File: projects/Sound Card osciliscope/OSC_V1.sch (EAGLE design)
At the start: 11 parts, among them X1 22-23-2021, X2 22-23-2021

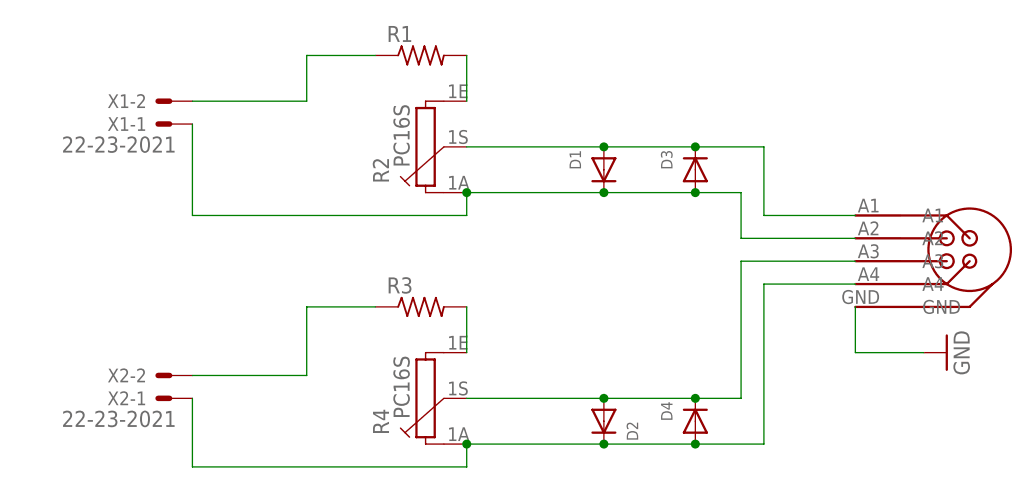
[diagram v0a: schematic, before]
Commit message: Update Library and Sccope
Added 3pin Jack to Library and finished up with the osciliscope
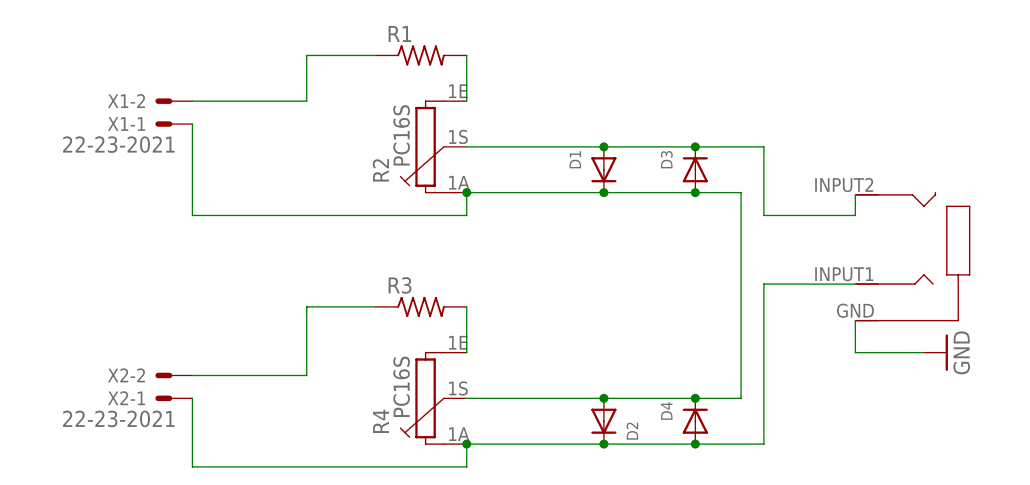
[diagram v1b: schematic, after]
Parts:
- U$1: value AUDIO5PIN -> AUDIO3PIN; device Test:AUDIO5PIN -> Test:AUDIO3PIN; OC_NEWARK unknown -> (none)
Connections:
- removed net N$7: D2.A, D4.C, R4.1S, U$1.A3
- net GND: now also D2.A, D4.C, R4.1S; no longer U$1.A2
- net N$3: now also U$1.INPUT2; no longer U$1.A1
- net N$8: now also U$1.INPUT1; no longer U$1.A4
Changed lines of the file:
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@@
-<attribute name="OC_NEWARK" value="unknown"/>
-</part>
-<part name="U$1" library="Test" deviceset="AUDIO5PIN" device="">
-<attribute name="MF" value=""/>
-<attribute name="MPN" value=""/>
 <attribute name="OC_NEWARK" value="unknown"/>
 </part>
@@
 <attribute name="OC_NEWARK" value="unknown"/>
 </part>
+<part name="U$1" library="Test" deviceset="AUDIO3PIN" device=""/>
 </parts>
 <sheets>
@@
 <attribute name="MPN" x="96.52" y="45.72" size="1.778" layer="96" display="off"/>
 </instance>
-<instance part="U$1" gate="G$1" x="127" y="63.5" smashed="yes">
-<attribute name="OC_NEWARK" x="127" y="63.5" size="1.778" layer="96" display="off"/>
-<attribute name="MF" x="127" y="63.5" size="1.778" layer="96" display="off"/>
-<attribute name="MPN" x="127" y="63.5" size="1.778" layer="96" display="off"/>
-</instance>
 <instance part="GND1" gate="1" x="124.46" y="53.34" smashed="yes" rot="R90">
 <attribute name="VALUE" x="127" y="50.8" size="1.778" layer="96" rot="R90"/>
@@
 <attribute name="MPN" x="86.36" y="45.72" size="1.778" layer="96" display="off"/>
 </instance>
+<instance part="U$1" gate="G$1" x="127" y="71.12" smashed="yes" rot="R180"/>
 </instances>
 <busses>
@@
 <net name="GND" class="0">
 <segment>
-<pinref part="U$1" gate="G$1" pin="GND"/>
-<wire x1="114.3" y1="58.42" x2="114.3" y2="53.34" width="0.1524" layer="91"/>
+<wire x1="114.3" y1="56.896" x2="114.3" y2="53.34" width="0.1524" layer="91"/>
 <wire x1="114.3" y1="53.34" x2="121.92" y2="53.34" width="0.1524" layer="91"/>
 <pinref part="GND1" gate="1" pin="GND"/>
+<pinref part="U$1" gate="G$1" pin="GND"/>
 </segment>
 <segment>
@@
 <wire x1="86.36" y1="71.12" x2="96.52" y2="71.12" width="0.1524" layer="91"/>
 <wire x1="96.52" y1="71.12" x2="101.6" y2="71.12" width="0.1524" layer="91"/>
-<wire x1="101.6" y1="71.12" x2="101.6" y2="66.04" width="0.1524" layer="91"/>
 <junction x="71.12" y="71.12"/>
-<pinref part="U$1" gate="G$1" pin="A2"/>
-<wire x1="101.6" y1="66.04" x2="114.3" y2="66.04" width="0.1524" layer="91"/>
 <pinref part="D1" gate="G$1" pin="C"/>
 <junction x="86.36" y="71.12"/>
 <pinref part="D3" gate="G$1" pin="A"/>
 <junction x="96.52" y="71.12"/>
-</segment>
-</net>
-<net name="N$1" class="0">
-<segment>
-<pinref part="X1" gate="-2" pin="S"/>
-<wire x1="40.64" y1="81.28" x2="53.34" y2="81.28" width="0.1524" layer="91"/>
-<wire x1="53.34" y1="81.28" x2="53.34" y2="86.36" width="0.1524" layer="91"/>
-<pinref part="R1" gate="G$1" pin="1"/>
-<wire x1="53.34" y1="86.36" x2="60.96" y2="86.36" width="0.1524" layer="91"/>
-</segment>
-</net>
-<net name="N$2" class="0">
-<segment>
-<pinref part="R1" gate="G$1" pin="2"/>
-<pinref part="R2" gate="G$1" pin="1E"/>
-<wire x1="71.12" y1="86.36" x2="71.12" y2="81.28" width="0.1524" layer="91"/>
-</segment>
-</net>
-<net name="N$3" class="0">
-<segment>
-<pinref part="R2" gate="G$1" pin="1S"/>
-<wire x1="71.12" y1="76.2" x2="86.36" y2="76.2" width="0.1524" layer="91"/>
-<wire x1="86.36" y1="76.2" x2="96.52" y2="76.2" width="0.1524" layer="91"/>
-<wire x1="96.52" y1="76.2" x2="104.14" y2="76.2" width="0.1524" layer="91"/>
-<wire x1="104.14" y1="76.2" x2="104.14" y2="68.58" width="0.1524" layer="91"/>
-<pinref part="U$1" gate="G$1" pin="A1"/>
-<wire x1="104.14" y1="68.58" x2="114.3" y2="68.58" width="0.1524" layer="91"/>
-<pinref part="D1" gate="G$1" pin="A"/>
-<junction x="86.36" y="76.2"/>
-<pinref part="D3" gate="G$1" pin="C"/>
-<junction x="96.52" y="76.2"/>
-</segment>
-</net>
-<net name="N$5" class="0">
-<segment>
-<pinref part="X2" gate="-2" pin="S"/>
-<wire x1="40.64" y1="50.8" x2="53.34" y2="50.8" width="0.1524" layer="91"/>
-<wire x1="53.34" y1="50.8" x2="53.34" y2="58.42" width="0.1524" layer="91"/>
-<pinref part="R3" gate="G$1" pin="1"/>
-<wire x1="53.34" y1="58.42" x2="60.96" y2="58.42" width="0.1524" layer="91"/>
-</segment>
-</net>
-<net name="N$6" class="0">
-<segment>
-<pinref part="R3" gate="G$1" pin="2"/>
-<pinref part="R4" gate="G$1" pin="1E"/>
-<wire x1="71.12" y1="58.42" x2="71.12" y2="53.34" width="0.1524" layer="91"/>
-</segment>
-</net>
-<net name="N$7" class="0">
-<segment>
 <pinref part="R4" gate="G$1" pin="1S"/>
 <pinref part="D2" gate="G$1" pin="A"/>
@@
 <junction x="86.36" y="48.26"/>
 <wire x1="96.52" y1="48.26" x2="101.6" y2="48.26" width="0.1524" layer="91"/>
-<wire x1="101.6" y1="48.26" x2="101.6" y2="63.5" width="0.1524" layer="91"/>
+<wire x1="101.6" y1="48.26" x2="101.6" y2="71.12" width="0.1524" layer="91"/>
 <junction x="96.52" y="48.26"/>
-<pinref part="U$1" gate="G$1" pin="A3"/>
-<wire x1="101.6" y1="63.5" x2="114.3" y2="63.5" width="0.1524" layer="91"/>
+</segment>
+</net>
+<net name="N$1" class="0">
+<segment>
+<pinref part="X1" gate="-2" pin="S"/>
+<wire x1="40.64" y1="81.28" x2="53.34" y2="81.28" width="0.1524" layer="91"/>
+<wire x1="53.34" y1="81.28" x2="53.34" y2="86.36" width="0.1524" layer="91"/>
+<pinref part="R1" gate="G$1" pin="1"/>
+<wire x1="53.34" y1="86.36" x2="60.96" y2="86.36" width="0.1524" layer="91"/>
+</segment>
+</net>
+<net name="N$2" class="0">
+<segment>
+<pinref part="R1" gate="G$1" pin="2"/>
+<pinref part="R2" gate="G$1" pin="1E"/>
+<wire x1="71.12" y1="86.36" x2="71.12" y2="81.28" width="0.1524" layer="91"/>
+</segment>
+</net>
+<net name="N$3" class="0">
+<segment>
+<pinref part="R2" gate="G$1" pin="1S"/>
+<wire x1="71.12" y1="76.2" x2="86.36" y2="76.2" width="0.1524" layer="91"/>
+<wire x1="86.36" y1="76.2" x2="96.52" y2="76.2" width="0.1524" layer="91"/>
+<wire x1="96.52" y1="76.2" x2="104.14" y2="76.2" width="0.1524" layer="91"/>
+<wire x1="104.14" y1="76.2" x2="104.14" y2="68.58" width="0.1524" layer="91"/>
+<wire x1="104.14" y1="68.58" x2="114.3" y2="68.58" width="0.1524" layer="91"/>
+<pinref part="D1" gate="G$1" pin="A"/>
+<junction x="86.36" y="76.2"/>
+<pinref part="D3" gate="G$1" pin="C"/>
+<junction x="96.52" y="76.2"/>
+<pinref part="U$1" gate="G$1" pin="INPUT2"/>
+<wire x1="114.3" y1="68.58" x2="114.3" y2="70.866" width="0.1524" layer="91"/>
+</segment>
+</net>
+<net name="N$5" class="0">
+<segment>
+<pinref part="X2" gate="-2" pin="S"/>
+<wire x1="40.64" y1="50.8" x2="53.34" y2="50.8" width="0.1524" layer="91"/>
+<wire x1="53.34" y1="50.8" x2="53.34" y2="58.42" width="0.1524" layer="91"/>
+<pinref part="R3" gate="G$1" pin="1"/>
+<wire x1="53.34" y1="58.42" x2="60.96" y2="58.42" width="0.1524" layer="91"/>
+</segment>
+</net>
+<net name="N$6" class="0">
+<segment>
+<pinref part="R3" gate="G$1" pin="2"/>
+<pinref part="R4" gate="G$1" pin="1E"/>
+<wire x1="71.12" y1="58.42" x2="71.12" y2="53.34" width="0.1524" layer="91"/>
 </segment>
 </net>
@@
 <wire x1="96.52" y1="43.18" x2="104.14" y2="43.18" width="0.1524" layer="91"/>
 <wire x1="104.14" y1="43.18" x2="104.14" y2="60.96" width="0.1524" layer="91"/>
-<pinref part="U$1" gate="G$1" pin="A4"/>
 <wire x1="104.14" y1="60.96" x2="114.3" y2="60.96" width="0.1524" layer="91"/>
 <pinref part="D4" gate="G$1" pin="A"/>
@@
 <wire x1="71.12" y1="40.64" x2="71.12" y2="43.18" width="0.1524" layer="91"/>
 <junction x="71.12" y="43.18"/>
+<pinref part="U$1" gate="G$1" pin="INPUT1"/>
 </segment>
 </net>
@@
 packages will not be understood (or retained) with this version.
 </note>
-<note version="8.5" severity="warning">
-Since Version 8.5, EAGLE supports locking for holes, vias, wires and polygons.
-The locking property on all objects of these types will not be understood in this version.
-</note>
 </compatibility>

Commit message: Updated board
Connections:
- net GND: now also D2.C, D4.A, R4.1A, X2-1.S; no longer D2.A, D4.C, R4.1S
- net N$8: now also D2.A, D4.C, R4.1S; no longer D2.C, D4.A, R4.1A, X2-1.S
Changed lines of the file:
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@@
 <setting verticaltext="up"/>
 </settings>
-<grid distance="0.1" unitdist="inch" unit="inch" style="lines" multiple="1" display="no" altdistance="0.01" altunitdist="inch" altunit="inch"/>
+<grid distance="0.1" unitdist="inch" unit="inch" style="lines" multiple="1" display="yes" altdistance="0.01" altunitdist="inch" altunit="inch"/>
 <layers>
 <layer number="1" name="Top" color="4" fill="1" visible="no" active="no"/>
@@
 <net name="GND" class="0">
 <segment>
-<wire x1="114.3" y1="56.896" x2="114.3" y2="53.34" width="0.1524" layer="91"/>
+<wire x1="114.3" y1="56.896" x2="114.3" y2="55.88" width="0.1524" layer="91"/>
+<wire x1="114.3" y1="55.88" x2="114.3" y2="53.34" width="0.1524" layer="91"/>
 <wire x1="114.3" y1="53.34" x2="121.92" y2="53.34" width="0.1524" layer="91"/>
 <pinref part="GND1" gate="1" pin="GND"/>
 <pinref part="U$1" gate="G$1" pin="GND"/>
-</segment>
-<segment>
 <pinref part="X1" gate="-1" pin="S"/>
-<wire x1="40.64" y1="78.74" x2="40.64" y2="68.58" width="0.1524" layer="91"/>
-<wire x1="40.64" y1="68.58" x2="71.12" y2="68.58" width="0.1524" layer="91"/>
+<wire x1="40.64" y1="78.74" x2="48.26" y2="78.74" width="0.1524" layer="91"/>
+<wire x1="48.26" y1="78.74" x2="48.26" y2="68.58" width="0.1524" layer="91"/>
 <pinref part="R2" gate="G$1" pin="1A"/>
+<wire x1="48.26" y1="68.58" x2="71.12" y2="68.58" width="0.1524" layer="91"/>
 <wire x1="71.12" y1="68.58" x2="71.12" y2="71.12" width="0.1524" layer="91"/>
 <wire x1="71.12" y1="71.12" x2="86.36" y2="71.12" width="0.1524" layer="91"/>
 <wire x1="86.36" y1="71.12" x2="96.52" y2="71.12" width="0.1524" layer="91"/>
-<wire x1="96.52" y1="71.12" x2="101.6" y2="71.12" width="0.1524" layer="91"/>
+<wire x1="96.52" y1="71.12" x2="106.68" y2="71.12" width="0.1524" layer="91"/>
+<wire x1="106.68" y1="71.12" x2="106.68" y2="55.88" width="0.1524" layer="91"/>
 <junction x="71.12" y="71.12"/>
+<wire x1="106.68" y1="55.88" x2="114.3" y2="55.88" width="0.1524" layer="91"/>
+<junction x="114.3" y="55.88"/>
 <pinref part="D1" gate="G$1" pin="C"/>
 <junction x="86.36" y="71.12"/>
 <pinref part="D3" gate="G$1" pin="A"/>
 <junction x="96.52" y="71.12"/>
-<pinref part="R4" gate="G$1" pin="1S"/>
-<pinref part="D2" gate="G$1" pin="A"/>
-<wire x1="71.12" y1="48.26" x2="86.36" y2="48.26" width="0.1524" layer="91"/>
-<pinref part="D4" gate="G$1" pin="C"/>
-<wire x1="86.36" y1="48.26" x2="96.52" y2="48.26" width="0.1524" layer="91"/>
-<junction x="86.36" y="48.26"/>
-<wire x1="96.52" y1="48.26" x2="101.6" y2="48.26" width="0.1524" layer="91"/>
-<wire x1="101.6" y1="48.26" x2="101.6" y2="71.12" width="0.1524" layer="91"/>
-<junction x="96.52" y="48.26"/>
+<pinref part="X2" gate="-1" pin="S"/>
+<wire x1="40.64" y1="48.26" x2="48.26" y2="48.26" width="0.1524" layer="91"/>
+<wire x1="48.26" y1="48.26" x2="48.26" y2="40.64" width="0.1524" layer="91"/>
+<pinref part="R4" gate="G$1" pin="1A"/>
+<wire x1="48.26" y1="40.64" x2="71.12" y2="40.64" width="0.1524" layer="91"/>
+<wire x1="71.12" y1="40.64" x2="71.12" y2="43.18" width="0.1524" layer="91"/>
+<wire x1="71.12" y1="43.18" x2="86.36" y2="43.18" width="0.1524" layer="91"/>
+<wire x1="86.36" y1="43.18" x2="96.52" y2="43.18" width="0.1524" layer="91"/>
+<wire x1="96.52" y1="43.18" x2="114.3" y2="43.18" width="0.1524" layer="91"/>
+<wire x1="114.3" y1="43.18" x2="114.3" y2="55.88" width="0.1524" layer="91"/>
+<junction x="71.12" y="43.18"/>
+<pinref part="D4" gate="G$1" pin="A"/>
+<junction x="96.52" y="43.18"/>
+<pinref part="D2" gate="G$1" pin="C"/>
+<junction x="86.36" y="43.18"/>
 </segment>
 </net>
@@
 <segment>
 <pinref part="X1" gate="-2" pin="S"/>
-<wire x1="40.64" y1="81.28" x2="53.34" y2="81.28" width="0.1524" layer="91"/>
-<wire x1="53.34" y1="81.28" x2="53.34" y2="86.36" width="0.1524" layer="91"/>
 <pinref part="R1" gate="G$1" pin="1"/>
-<wire x1="53.34" y1="86.36" x2="60.96" y2="86.36" width="0.1524" layer="91"/>
+<wire x1="40.64" y1="81.28" x2="60.96" y2="81.28" width="0.1524" layer="91"/>
+<wire x1="60.96" y1="81.28" x2="60.96" y2="86.36" width="0.1524" layer="91"/>
 </segment>
 </net>
@@
 </segment>
 </net>
-<net name="N$3" class="0">
+<net name="N$4" class="0">
 <segment>
 <pinref part="R2" gate="G$1" pin="1S"/>
+<pinref part="U$1" gate="G$1" pin="INPUT2"/>
 <wire x1="71.12" y1="76.2" x2="86.36" y2="76.2" width="0.1524" layer="91"/>
 <wire x1="86.36" y1="76.2" x2="96.52" y2="76.2" width="0.1524" layer="91"/>
-<wire x1="96.52" y1="76.2" x2="104.14" y2="76.2" width="0.1524" layer="91"/>
-<wire x1="104.14" y1="76.2" x2="104.14" y2="68.58" width="0.1524" layer="91"/>
-<wire x1="104.14" y1="68.58" x2="114.3" y2="68.58" width="0.1524" layer="91"/>
+<wire x1="96.52" y1="76.2" x2="114.3" y2="76.2" width="0.1524" layer="91"/>
+<wire x1="114.3" y1="76.2" x2="114.3" y2="70.866" width="0.1524" layer="91"/>
 <pinref part="D1" gate="G$1" pin="A"/>
 <junction x="86.36" y="76.2"/>
 <pinref part="D3" gate="G$1" pin="C"/>
 <junction x="96.52" y="76.2"/>
-<pinref part="U$1" gate="G$1" pin="INPUT2"/>
-<wire x1="114.3" y1="68.58" x2="114.3" y2="70.866" width="0.1524" layer="91"/>
 </segment>
 </net>
@@
 <segment>
 <pinref part="X2" gate="-2" pin="S"/>
-<wire x1="40.64" y1="50.8" x2="53.34" y2="50.8" width="0.1524" layer="91"/>
-<wire x1="53.34" y1="50.8" x2="53.34" y2="58.42" width="0.1524" layer="91"/>
 <pinref part="R3" gate="G$1" pin="1"/>
-<wire x1="53.34" y1="58.42" x2="60.96" y2="58.42" width="0.1524" layer="91"/>
+<wire x1="40.64" y1="50.8" x2="60.96" y2="50.8" width="0.1524" layer="91"/>
+<wire x1="60.96" y1="50.8" x2="60.96" y2="58.42" width="0.1524" layer="91"/>
 </segment>
 </net>
@@
 <net name="N$8" class="0">
 <segment>
-<pinref part="R4" gate="G$1" pin="1A"/>
-<wire x1="71.12" y1="43.18" x2="86.36" y2="43.18" width="0.1524" layer="91"/>
-<wire x1="86.36" y1="43.18" x2="96.52" y2="43.18" width="0.1524" layer="91"/>
-<wire x1="96.52" y1="43.18" x2="104.14" y2="43.18" width="0.1524" layer="91"/>
-<wire x1="104.14" y1="43.18" x2="104.14" y2="60.96" width="0.1524" layer="91"/>
-<wire x1="104.14" y1="60.96" x2="114.3" y2="60.96" width="0.1524" layer="91"/>
-<pinref part="D4" gate="G$1" pin="A"/>
-<junction x="96.52" y="43.18"/>
-<pinref part="D2" gate="G$1" pin="C"/>
-<junction x="86.36" y="43.18"/>
-<pinref part="X2" gate="-1" pin="S"/>
-<wire x1="40.64" y1="48.26" x2="40.64" y2="40.64" width="0.1524" layer="91"/>
-<wire x1="40.64" y1="40.64" x2="71.12" y2="40.64" width="0.1524" layer="91"/>
-<wire x1="71.12" y1="40.64" x2="71.12" y2="43.18" width="0.1524" layer="91"/>
-<junction x="71.12" y="43.18"/>
+<pinref part="R4" gate="G$1" pin="1S"/>
+<wire x1="71.12" y1="48.26" x2="86.36" y2="48.26" width="0.1524" layer="91"/>
+<wire x1="86.36" y1="48.26" x2="96.52" y2="48.26" width="0.1524" layer="91"/>
+<wire x1="96.52" y1="48.26" x2="109.22" y2="48.26" width="0.1524" layer="91"/>
+<wire x1="109.22" y1="48.26" x2="109.22" y2="60.96" width="0.1524" layer="91"/>
 <pinref part="U$1" gate="G$1" pin="INPUT1"/>
-</segment>
-</net>
+<wire x1="109.22" y1="60.96" x2="114.3" y2="60.96" width="0.1524" layer="91"/>
+<pinref part="D4" gate="G$1" pin="C"/>
+<junction x="96.52" y="48.26"/>
+<pinref part="D2" gate="G$1" pin="A"/>
+<junction x="86.36" y="48.26"/>
+</segment>
+</net>
